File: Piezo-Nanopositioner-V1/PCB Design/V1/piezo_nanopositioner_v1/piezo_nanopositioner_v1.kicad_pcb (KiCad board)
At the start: 2 copper layers, 187.2 x 72.2 mm, 101 parts, among them J101 Conn_01x03_Pin, J201 Conn_01x10_Pin, J202 RF2-04A-T-00-50-G, J301 Conn_01x10_Pin, J302 RF2-04A-T-00-50-G, J401 Conn_01x10_Pin, J402 RF2-04A-T-00-50-G, U201 TL431AIDBZR, U202 DAC0800LCM, U203 TDA2050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

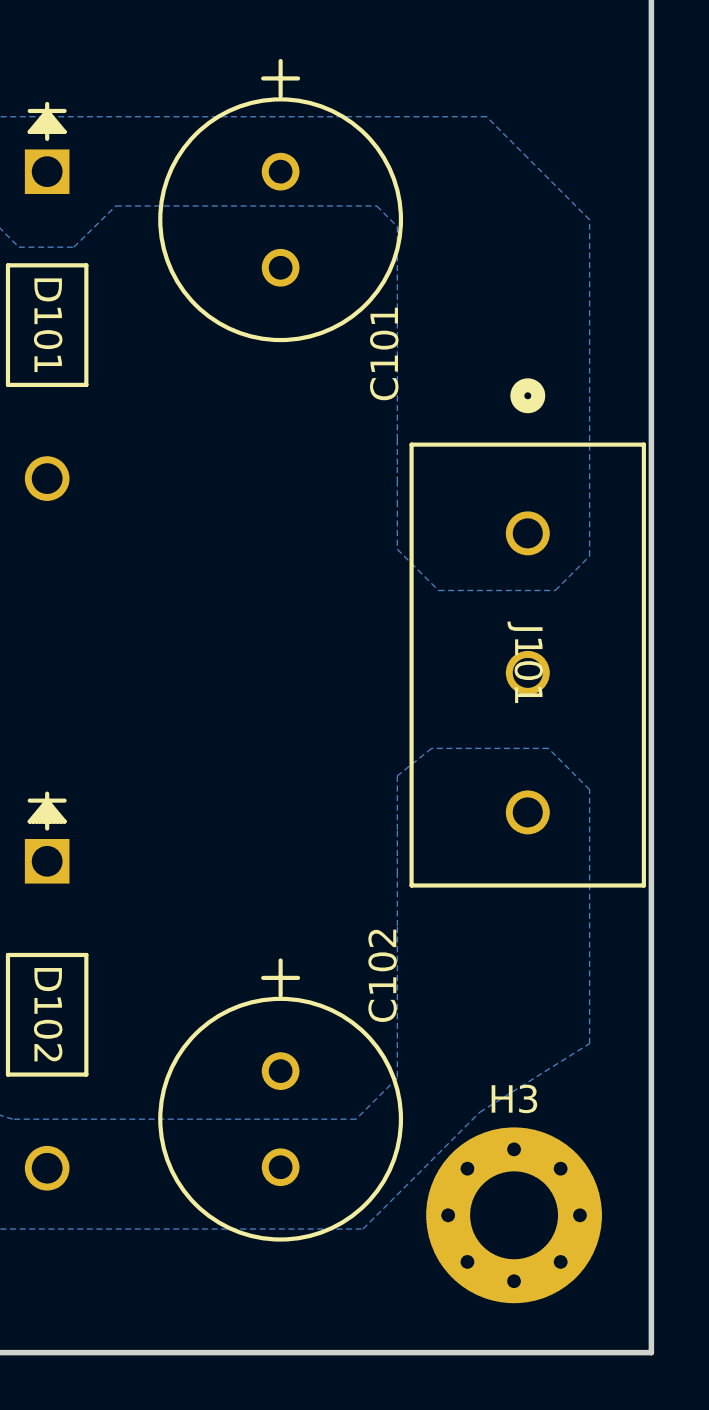
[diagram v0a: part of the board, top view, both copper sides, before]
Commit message: added GND,+/-15V to silkscreen.
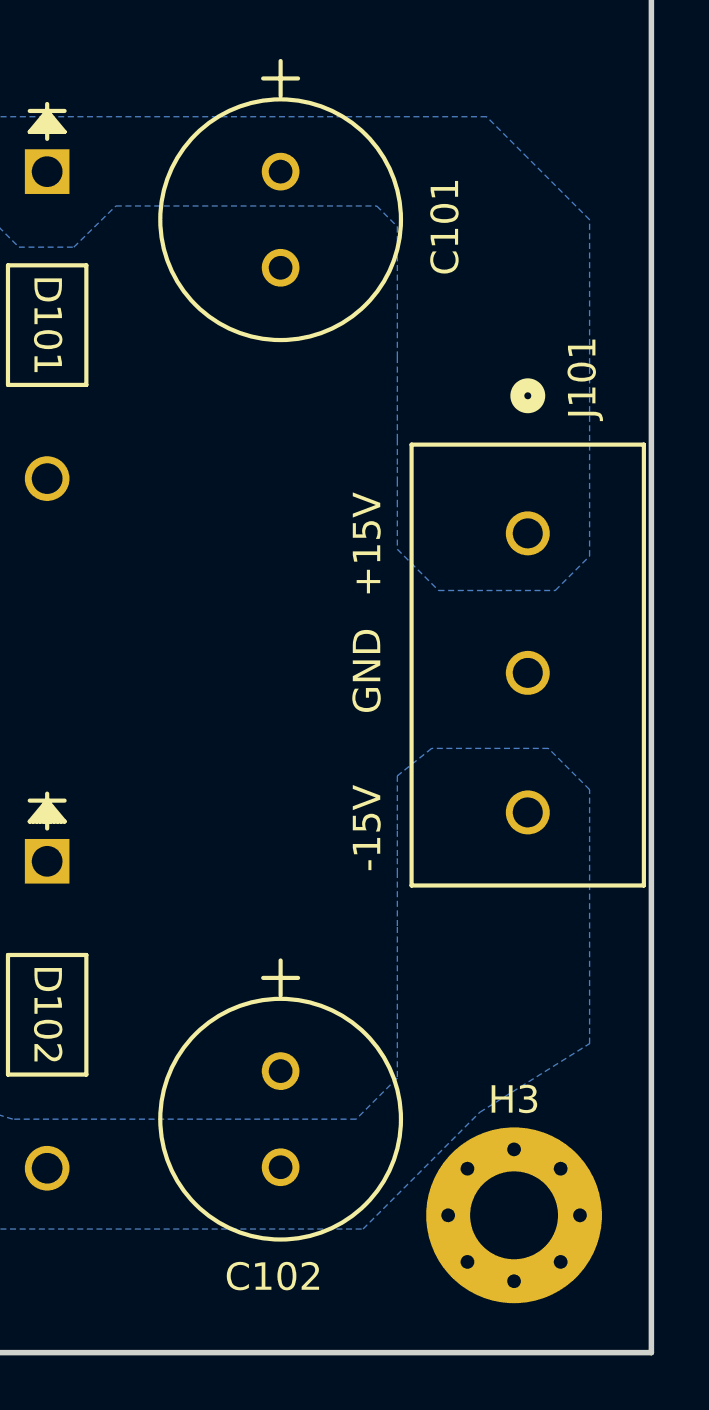
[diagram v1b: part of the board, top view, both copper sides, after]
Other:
- board text added: "+15V"
- board text added: "-15V"
- board text added: "GND"

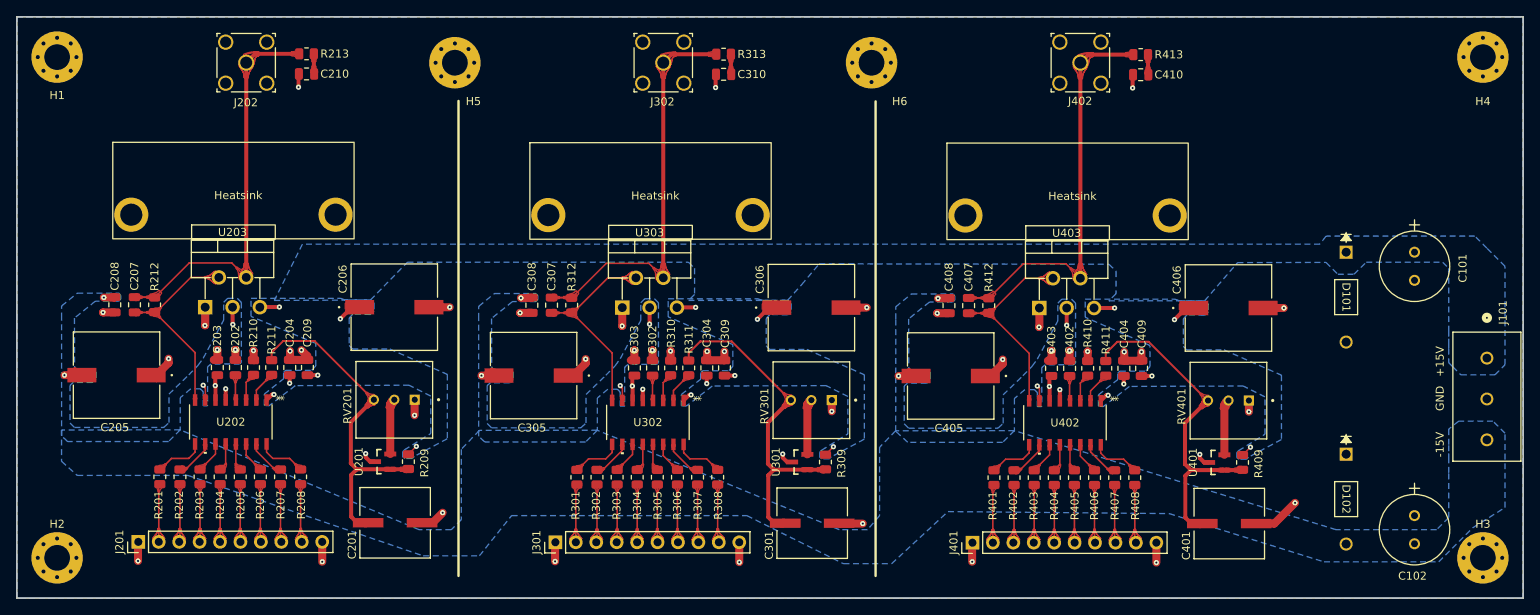
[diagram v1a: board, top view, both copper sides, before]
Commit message: Fixed ground plane issue (ground loop found). Solution was to move from a 2 layer PCB to 4 layer PCB. Will cost extra but signal integrity will benefit.
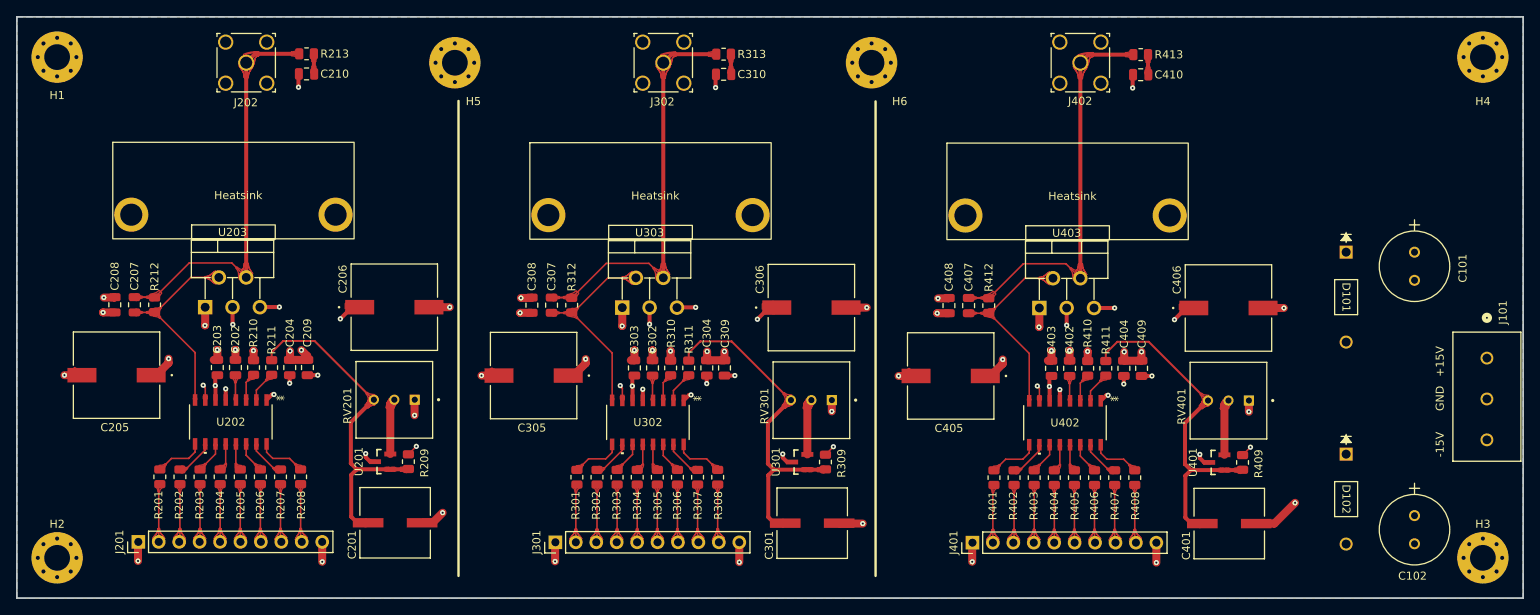
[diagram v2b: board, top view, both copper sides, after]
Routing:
- added copper zone on In2.Cu, net +15V
- added copper zone on In2.Cu, net -15V
- added copper zone on In1.Cu, net GND
- removed copper zone on B.Cu, net +15V
- removed copper zone on B.Cu, net -15V
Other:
- copper layers 2 -> 4
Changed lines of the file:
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@@
 	(layers
 		(0 "F.Cu" signal)
+		(1 "In1.Cu" signal)
+		(2 "In2.Cu" signal)
 		(31 "B.Cu" signal)
 		(32 "B.Adhes" user "B.Adhesive")
@@
 			)
 			(layer "dielectric 1"
+				(type "prepreg")
+				(thickness 0.1)
+				(material "FR4")
+				(epsilon_r 4.5)
+				(loss_tangent 0.02)
+			)
+			(layer "In1.Cu"
+				(type "copper")
+				(thickness 0.035)
+			)
+			(layer "dielectric 2"
 				(type "core")
-				(thickness 1.51)
+				(thickness 1.24)
+				(material "FR4")
+				(epsilon_r 4.5)
+				(loss_tangent 0.02)
+			)
+			(layer "In2.Cu"
+				(type "copper")
+				(thickness 0.035)
+			)
+			(layer "dielectric 3"
+				(type "prepreg")
+				(thickness 0.1)
 				(material "FR4")
 				(epsilon_r 4.5)
@@
 	)
 	(zone
+		(net 2)
+		(net_name "GND")
+		(layers "In1.Cu" "B.Cu")
+		(hatch edge 0.5)
+		(connect_pads
+			(clearance 0.5)
+		)
+		(min_thickness 0.25)
+		(filled_areas_thickness no)
+		(fill yes
+			(thermal_gap 0.5)
+			(thermal_bridge_width 0.5)
+		)
+		(polygon
+			(pts
+				(xy 257.5 115.75) (xy 70.25 115.75) (xy 70.25 43.5) (xy 257.5 43.5)
+			)
+		)
+	)
+	(zone
 		(net 3)
 		(net_name "-15V")
-		(layer "B.Cu")
+		(layer "In2.Cu")
 		(hatch edge 0.5)
 		(priority 2)
@@
 		(net 1)
 		(net_name "+15V")
-		(layer "B.Cu")
+		(layer "In2.Cu")
 		(hatch edge 0.5)
 		(priority 2)
@@
 		(net 1)
 		(net_name "+15V")
-		(layer "B.Cu")
+		(layer "In2.Cu")
 		(hatch edge 0.5)
 		(priority 2)
@@
 	)
 	(zone
-		(net 2)
-		(net_name "GND")
-		(layer "B.Cu")
-		(hatch edge 0.5)
-		(connect_pads
-			(clearance 0.5)
-		)
-		(min_thickness 0.25)
-		(filled_areas_thickness no)
-		(fill yes
-			(thermal_gap 0.5)
-			(thermal_bridge_width 0.5)
-		)
-		(polygon
-			(pts
-				(xy 257.5 115.75) (xy 70.25 115.75) (xy 70.25 43.5) (xy 257.5 43.5)
-			)
-		)
-	)
-	(zone
 		(net 3)
 		(net_name "-15V")
-		(layer "B.Cu")
+		(layer "In2.Cu")
 		(hatch edge 0.5)
 		(priority 2)
@@
 		(net 1)
 		(net_name "+15V")
-		(layer "B.Cu")
+		(layer "In2.Cu")
 		(hatch edge 0.5)
 		(priority 2)
@@
 		(net 3)
 		(net_name "-15V")
-		(layer "B.Cu")
+		(layer "In2.Cu")
 		(hatch edge 0.5)
 		(priority 3)
@@
 		(net 1)
 		(net_name "+15V")
-		(layer "B.Cu")
+		(layer "In2.Cu")
 		(hatch edge 0.5)
 		(priority 1)
@@
 		(net 3)
 		(net_name "-15V")
-		(layer "B.Cu")
+		(layer "In2.Cu")
 		(hatch edge 0.5)
 		(priority 2)
